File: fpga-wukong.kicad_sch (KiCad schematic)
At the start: 2 parts, among them J4 QMTECH FPGA Module U4, J5 QMTECH FPGA Module U5

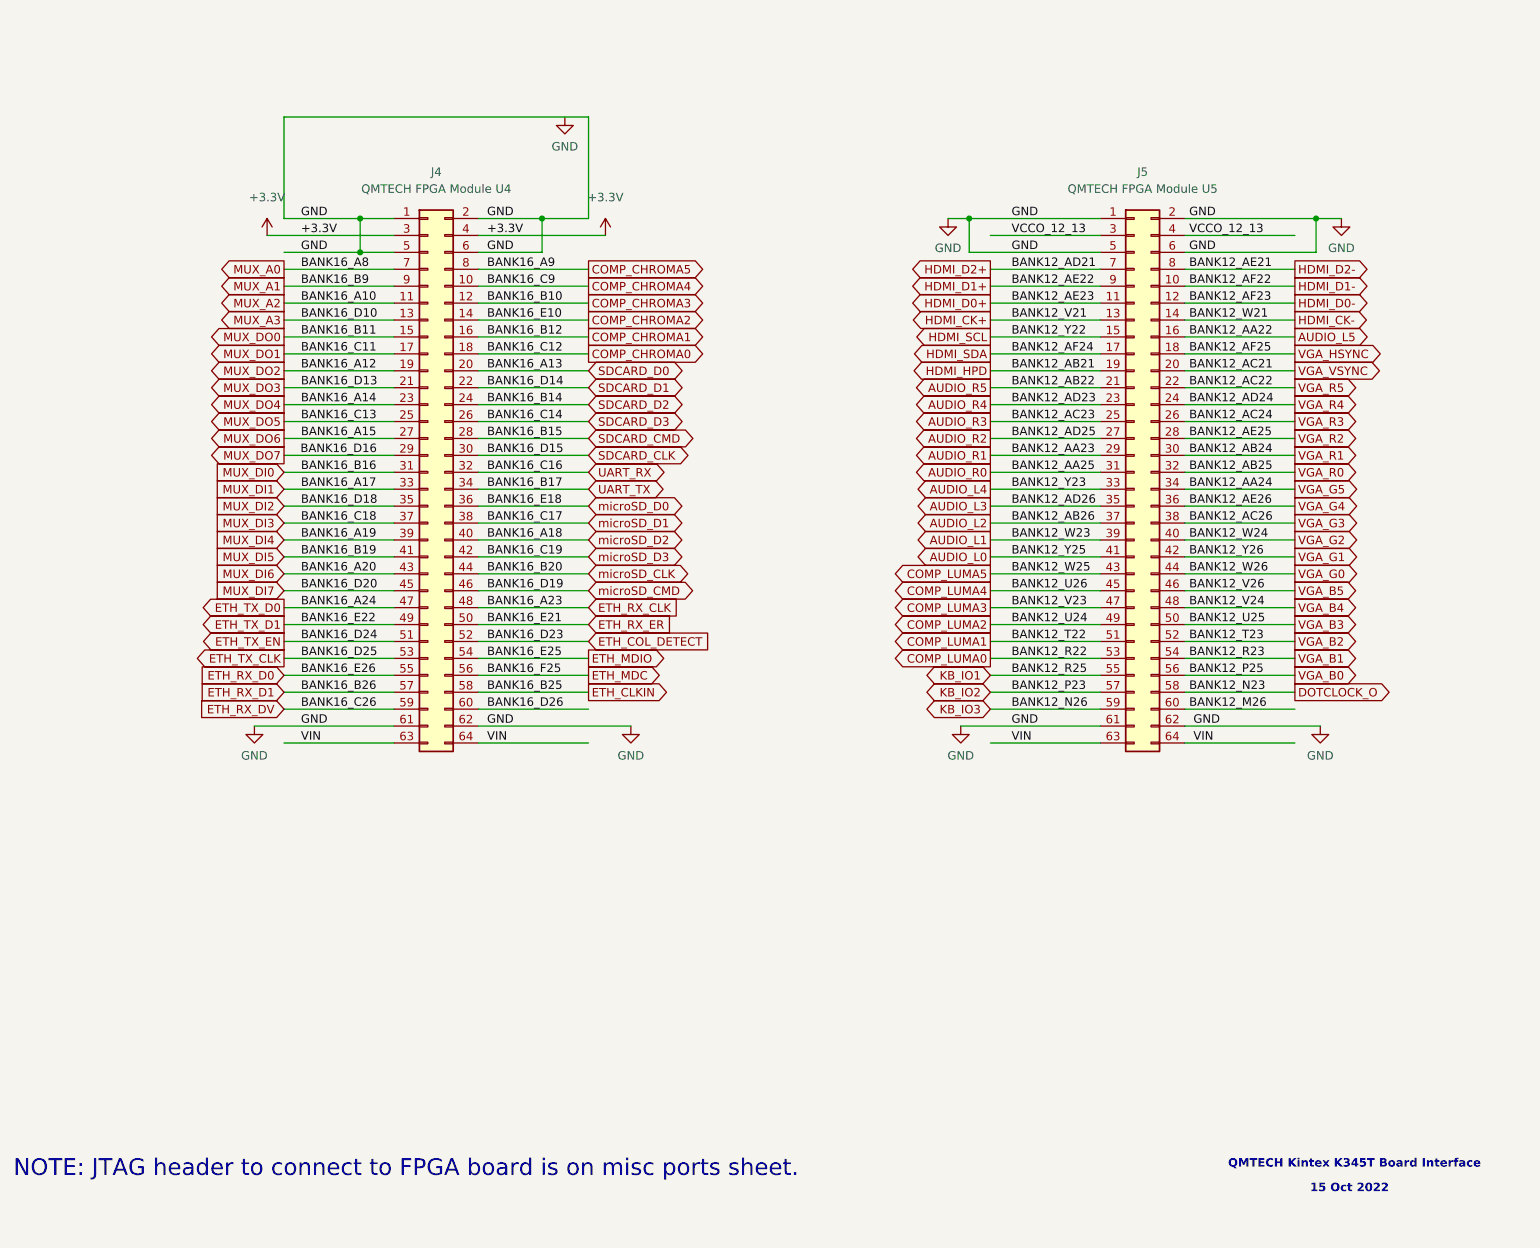
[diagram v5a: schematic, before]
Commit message: rearrange FPGA board connectors to detangle. Begin routing HDMI
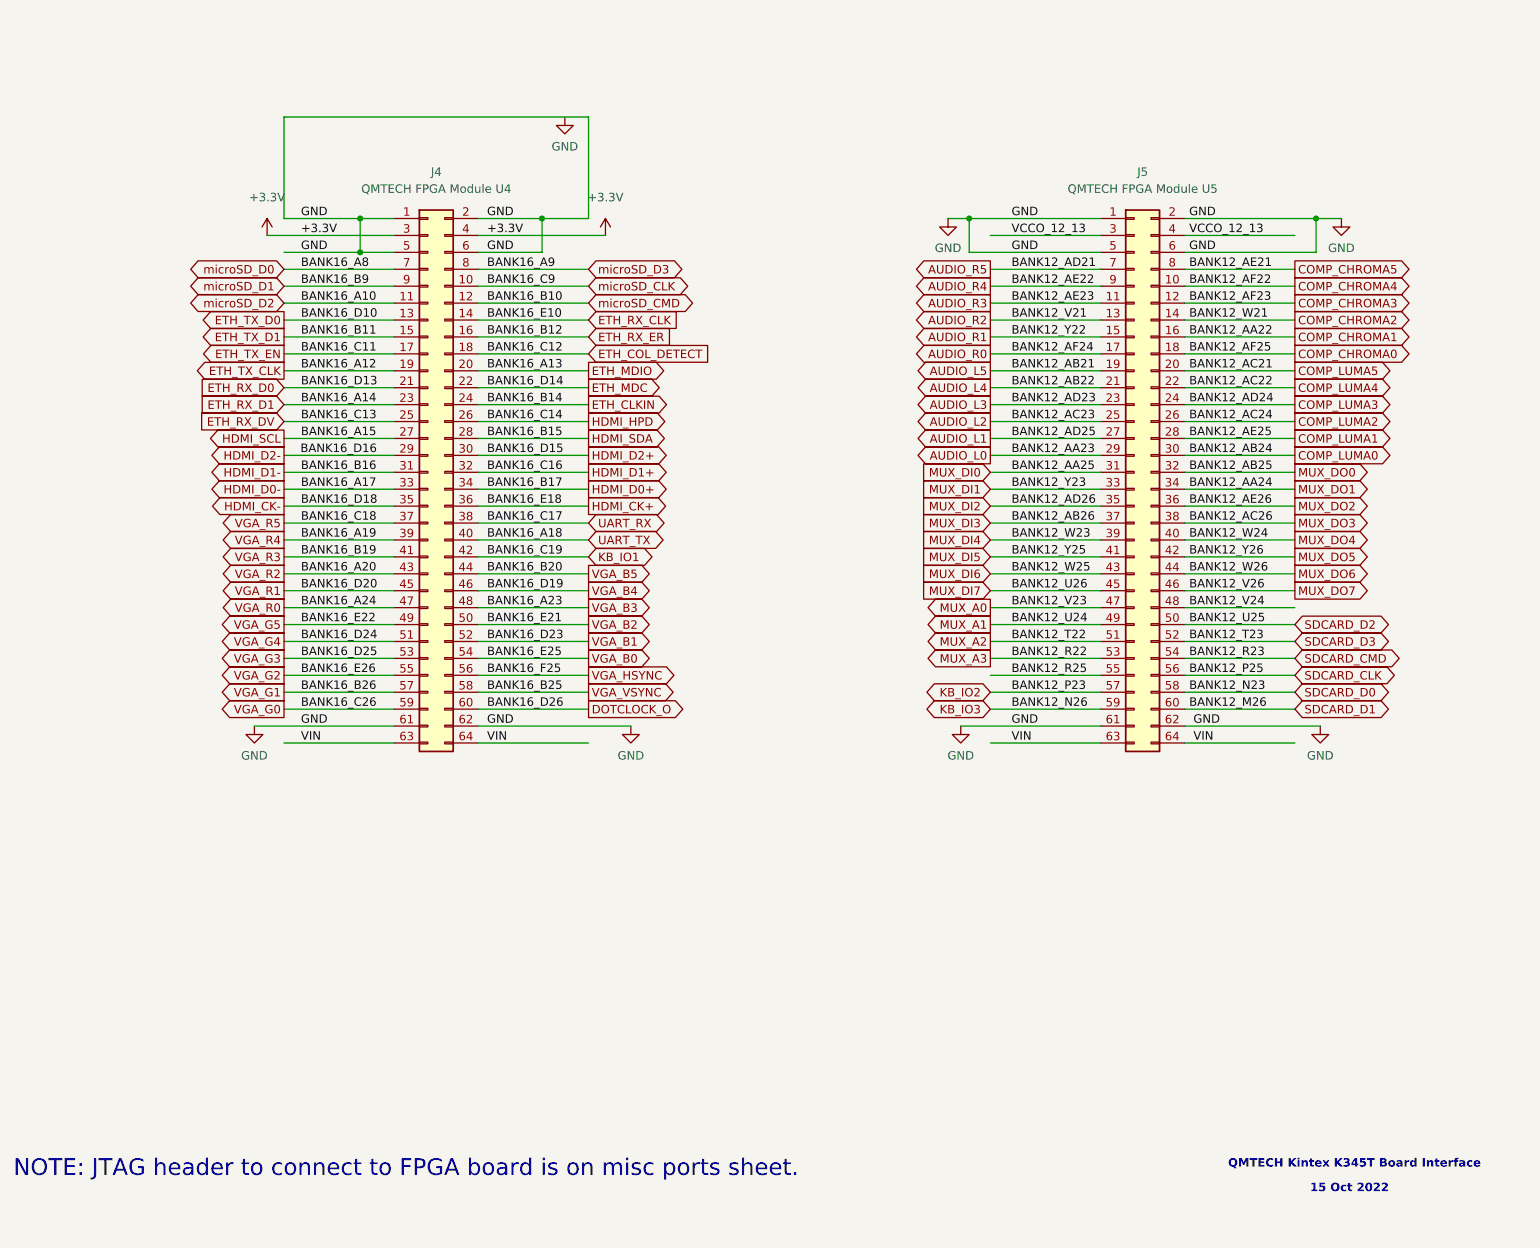
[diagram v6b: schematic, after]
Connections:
- net BANK12_M26 is gone; now on net SDCARD_D1: J5.60 (Pin_60)
- net BANK16_D26 is gone; now on net DOTCLOCK_O: J4.60 (Pin_60)
- net AUDIO_L0: now also J5.29 (Pin_29); no longer J5.41 (Pin_41)
- net AUDIO_L1: now also J5.27 (Pin_27); no longer J5.39 (Pin_39)
- net AUDIO_L2: now also J5.25 (Pin_25); no longer J5.37 (Pin_37)
- net AUDIO_L3: now also J5.23 (Pin_23); no longer J5.35 (Pin_35)
- net AUDIO_L4: now also J5.21 (Pin_21); no longer J5.33 (Pin_33)
- net AUDIO_L5: now also J5.19 (Pin_19); no longer J5.16 (Pin_16)
- net AUDIO_R0: now also J5.17 (Pin_17); no longer J5.31 (Pin_31)
- net AUDIO_R1: now also J5.15 (Pin_15); no longer J5.29 (Pin_29)
- net AUDIO_R2: now also J5.13 (Pin_13); no longer J5.27 (Pin_27)
- net AUDIO_R3: now also J5.11 (Pin_11); no longer J5.25 (Pin_25)
- net AUDIO_R4: now also J5.9 (Pin_9); no longer J5.23 (Pin_23)
- net AUDIO_R5: now also J5.7 (Pin_7); no longer J5.21 (Pin_21)
- net COMP_CHROMA0: now also J5.18 (Pin_18); no longer J4.18 (Pin_18)
- net COMP_CHROMA1: now also J5.16 (Pin_16); no longer J4.16 (Pin_16)
- net COMP_CHROMA2: now also J5.14 (Pin_14); no longer J4.14 (Pin_14)
- net COMP_CHROMA3: now also J5.12 (Pin_12); no longer J4.12 (Pin_12)
- net COMP_CHROMA4: now also J5.10 (Pin_10); no longer J4.10 (Pin_10)
- net COMP_CHROMA5: now also J5.8 (Pin_8); no longer J4.8 (Pin_8)
- net COMP_LUMA0: now also J5.30 (Pin_30); no longer J5.53 (Pin_53)
- net COMP_LUMA1: now also J5.28 (Pin_28); no longer J5.51 (Pin_51)
- net COMP_LUMA2: now also J5.26 (Pin_26); no longer J5.49 (Pin_49)
- net COMP_LUMA3: now also J5.24 (Pin_24); no longer J5.47 (Pin_47)
- net COMP_LUMA4: now also J5.22 (Pin_22); no longer J5.45 (Pin_45)
- net COMP_LUMA5: now also J5.20 (Pin_20); no longer J5.43 (Pin_43)
- net DOTCLOCK_O: no longer J5.58 (Pin_58)
- net ETH_CLKIN: now also J4.24 (Pin_24); no longer J4.58 (Pin_58)
- net ETH_COL_DETECT: now also J4.18 (Pin_18); no longer J4.52 (Pin_52)
- net ETH_MDC: now also J4.22 (Pin_22); no longer J4.56 (Pin_56)
- net ETH_MDIO: now also J4.20 (Pin_20); no longer J4.54 (Pin_54)
- net ETH_RX_CLK: now also J4.14 (Pin_14); no longer J4.48 (Pin_48)
- net ETH_RX_D0: now also J4.21 (Pin_21); no longer J4.55 (Pin_55)
- net ETH_RX_D1: now also J4.23 (Pin_23); no longer J4.57 (Pin_57)
- net ETH_RX_DV: now also J4.25 (Pin_25); no longer J4.59 (Pin_59)
- net ETH_RX_ER: now also J4.16 (Pin_16); no longer J4.50 (Pin_50)
- net ETH_TX_CLK: now also J4.19 (Pin_19); no longer J4.53 (Pin_53)
- net ETH_TX_D0: now also J4.13 (Pin_13); no longer J4.47 (Pin_47)
- net ETH_TX_D1: now also J4.15 (Pin_15); no longer J4.49 (Pin_49)
- net ETH_TX_EN: now also J4.17 (Pin_17); no longer J4.51 (Pin_51)
- net HDMI_CK+: now also J4.36 (Pin_36); no longer J5.13 (Pin_13)
- net HDMI_CK-: now also J4.35 (Pin_35); no longer J5.14 (Pin_14)
- net HDMI_D0+: now also J4.34 (Pin_34); no longer J5.11 (Pin_11)
- net HDMI_D0-: now also J4.33 (Pin_33); no longer J5.12 (Pin_12)
- net HDMI_D1+: now also J4.32 (Pin_32); no longer J5.9 (Pin_9)
- net HDMI_D1-: now also J4.31 (Pin_31); no longer J5.10 (Pin_10)
- net HDMI_D2+: now also J4.30 (Pin_30); no longer J5.7 (Pin_7)
- net HDMI_D2-: now also J4.29 (Pin_29); no longer J5.8 (Pin_8)
- net HDMI_HPD: now also J4.26 (Pin_26); no longer J5.19 (Pin_19)
- net HDMI_SCL: now also J4.27 (Pin_27); no longer J5.15 (Pin_15)
- net HDMI_SDA: now also J4.28 (Pin_28); no longer J5.17 (Pin_17)
- net KB_IO1: now also J4.42 (Pin_42); no longer J5.55 (Pin_55)
- net MUX_A0: now also J5.47 (Pin_47); no longer J4.7 (Pin_7)
- net MUX_A1: now also J5.49 (Pin_49); no longer J4.9 (Pin_9)
- net MUX_A2: now also J5.51 (Pin_51); no longer J4.11 (Pin_11)
- net MUX_A3: now also J5.53 (Pin_53); no longer J4.13 (Pin_13)
- net MUX_DI0: now also J5.31 (Pin_31); no longer J4.31 (Pin_31)
- net MUX_DI1: now also J5.33 (Pin_33); no longer J4.33 (Pin_33)
- net MUX_DI2: now also J5.35 (Pin_35); no longer J4.35 (Pin_35)
- net MUX_DI3: now also J5.37 (Pin_37); no longer J4.37 (Pin_37)
- net MUX_DI4: now also J5.39 (Pin_39); no longer J4.39 (Pin_39)
- net MUX_DI5: now also J5.41 (Pin_41); no longer J4.41 (Pin_41)
- net MUX_DI6: now also J5.43 (Pin_43); no longer J4.43 (Pin_43)
- net MUX_DI7: now also J5.45 (Pin_45); no longer J4.45 (Pin_45)
- net MUX_DO0: now also J5.32 (Pin_32); no longer J4.15 (Pin_15)
- net MUX_DO1: now also J5.34 (Pin_34); no longer J4.17 (Pin_17)
- net MUX_DO2: now also J5.36 (Pin_36); no longer J4.19 (Pin_19)
- net MUX_DO3: now also J5.38 (Pin_38); no longer J4.21 (Pin_21)
- net MUX_DO4: now also J5.40 (Pin_40); no longer J4.23 (Pin_23)
- net MUX_DO5: now also J5.42 (Pin_42); no longer J4.25 (Pin_25)
- net MUX_DO6: now also J5.44 (Pin_44); no longer J4.27 (Pin_27)
- net MUX_DO7: now also J5.46 (Pin_46); no longer J4.29 (Pin_29)
- net SDCARD_CLK: now also J5.56 (Pin_56); no longer J4.30 (Pin_30)
- net SDCARD_CMD: now also J5.54 (Pin_54); no longer J4.28 (Pin_28)
- net SDCARD_D0: now also J5.58 (Pin_58); no longer J4.20 (Pin_20)
- net SDCARD_D1: no longer J4.22 (Pin_22)
- net SDCARD_D2: now also J5.50 (Pin_50); no longer J4.24 (Pin_24)
- net SDCARD_D3: now also J5.52 (Pin_52); no longer J4.26 (Pin_26)
- net UART_RX: now also J4.38 (Pin_38); no longer J4.32 (Pin_32)
- net UART_TX: now also J4.40 (Pin_40); no longer J4.34 (Pin_34)
- net VGA_B0: now also J4.54 (Pin_54); no longer J5.56 (Pin_56)
- net VGA_B1: now also J4.52 (Pin_52); no longer J5.54 (Pin_54)
- net VGA_B2: now also J4.50 (Pin_50); no longer J5.52 (Pin_52)
- net VGA_B3: now also J4.48 (Pin_48); no longer J5.50 (Pin_50)
- net VGA_B4: now also J4.46 (Pin_46); no longer J5.48 (Pin_48)
- net VGA_B5: now also J4.44 (Pin_44); no longer J5.46 (Pin_46)
- net VGA_G0: now also J4.59 (Pin_59); no longer J5.44 (Pin_44)
- net VGA_G1: now also J4.57 (Pin_57); no longer J5.42 (Pin_42)
- net VGA_G2: now also J4.55 (Pin_55); no longer J5.40 (Pin_40)
- net VGA_G3: now also J4.53 (Pin_53); no longer J5.38 (Pin_38)
- net VGA_G4: now also J4.51 (Pin_51); no longer J5.36 (Pin_36)
- net VGA_G5: now also J4.49 (Pin_49); no longer J5.34 (Pin_34)
- net VGA_HSYNC: now also J4.56 (Pin_56); no longer J5.18 (Pin_18)
- net VGA_R0: now also J4.47 (Pin_47); no longer J5.32 (Pin_32)
- net VGA_R1: now also J4.45 (Pin_45); no longer J5.30 (Pin_30)
- net VGA_R2: now also J4.43 (Pin_43); no longer J5.28 (Pin_28)
- net VGA_R3: now also J4.41 (Pin_41); no longer J5.26 (Pin_26)
- net VGA_R4: now also J4.39 (Pin_39); no longer J5.24 (Pin_24)
- net VGA_R5: now also J4.37 (Pin_37); no longer J5.22 (Pin_22)
- net VGA_VSYNC: now also J4.58 (Pin_58); no longer J5.20 (Pin_20)
- net microSD_CLK: now also J4.10 (Pin_10); no longer J4.44 (Pin_44)
- net microSD_CMD: now also J4.12 (Pin_12); no longer J4.46 (Pin_46)
- net microSD_D0: now also J4.7 (Pin_7); no longer J4.36 (Pin_36)
- net microSD_D1: now also J4.9 (Pin_9); no longer J4.38 (Pin_38)
- net microSD_D2: now also J4.11 (Pin_11); no longer J4.40 (Pin_40)
- net microSD_D3: now also J4.8 (Pin_8); no longer J4.42 (Pin_42)
- new net BANK12_R25: J5.55 (Pin_55)
- new net BANK12_V24: J5.48 (Pin_48)

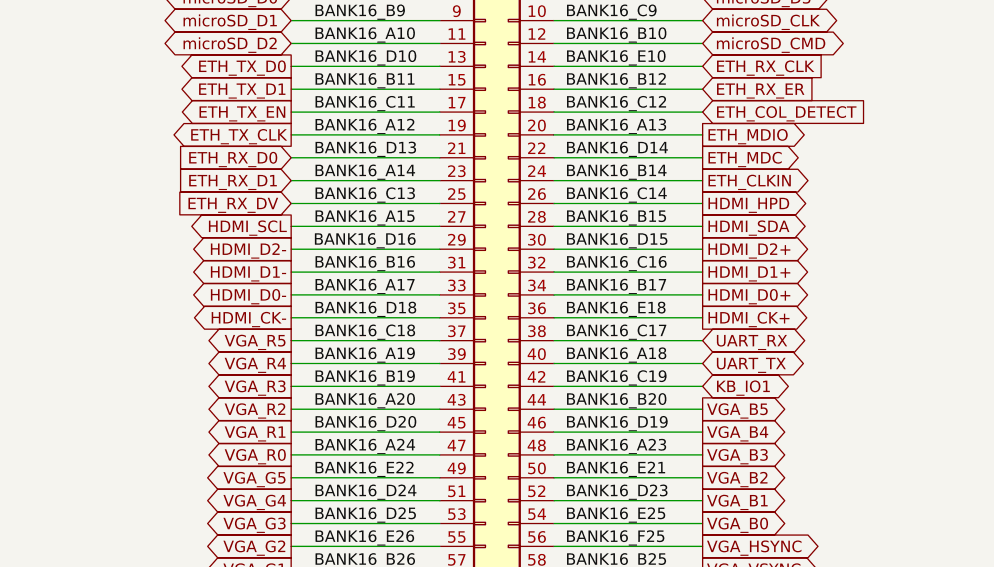
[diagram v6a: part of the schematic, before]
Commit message: Replace HDMI connector #13
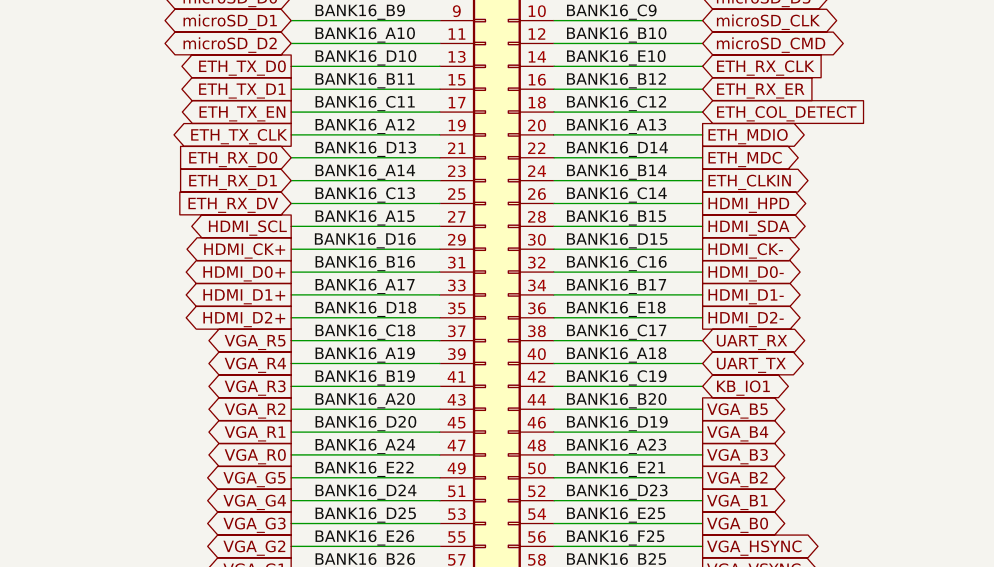
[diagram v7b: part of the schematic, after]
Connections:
- net HDMI_CK+: now also J4.29 (Pin_29); no longer J4.36 (Pin_36)
- net HDMI_CK-: now also J4.30 (Pin_30); no longer J4.35 (Pin_35)
- net HDMI_D0+: now also J4.31 (Pin_31); no longer J4.34 (Pin_34)
- net HDMI_D0-: now also J4.32 (Pin_32); no longer J4.33 (Pin_33)
- net HDMI_D1+: now also J4.33 (Pin_33); no longer J4.32 (Pin_32)
- net HDMI_D1-: now also J4.34 (Pin_34); no longer J4.31 (Pin_31)
- net HDMI_D2+: now also J4.35 (Pin_35); no longer J4.30 (Pin_30)
- net HDMI_D2-: now also J4.36 (Pin_36); no longer J4.29 (Pin_29)
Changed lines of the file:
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@@
     )
   )
-  (global_label "HDMI_D1-" (shape output) (at 60.325 85.725 180) (fields_autoplaced)
-    (effects (font (size 1.27 1.27)) (justify right))
-    (property "Intersheet References" "${INTERSHEET_REFS}" (id 0) (at 48.2357 85.6456 0)
-      (effects (font (size 1.27 1.27)) (justify right) hide)
+  (global_label "HDMI_D1-" (shape output) (at 106.045 88.265 0) (fields_autoplaced)
+    (effects (font (size 1.27 1.27)) (justify left))
+    (property "Intersheet References" "${INTERSHEET_REFS}" (id 0) (at 118.1343 88.3444 0)
+      (effects (font (size 1.27 1.27)) (justify left) hide)
     )
   )
@@
     )
   )
-  (global_label "HDMI_D0-" (shape output) (at 60.325 88.265 180) (fields_autoplaced)
-    (effects (font (size 1.27 1.27)) (justify right))
-    (property "Intersheet References" "${INTERSHEET_REFS}" (id 0) (at 48.2357 88.1856 0)
-      (effects (font (size 1.27 1.27)) (justify right) hide)
+  (global_label "HDMI_D0-" (shape output) (at 106.045 85.725 0) (fields_autoplaced)
+    (effects (font (size 1.27 1.27)) (justify left))
+    (property "Intersheet References" "${INTERSHEET_REFS}" (id 0) (at 118.1343 85.8044 0)
+      (effects (font (size 1.27 1.27)) (justify left) hide)
     )
   )
@@
     )
   )
-  (global_label "HDMI_D0+" (shape output) (at 106.045 88.265 0) (fields_autoplaced)
-    (effects (font (size 1.27 1.27)) (justify left))
-    (property "Intersheet References" "${INTERSHEET_REFS}" (id 0) (at 118.1343 88.1856 0)
-      (effects (font (size 1.27 1.27)) (justify left) hide)
+  (global_label "HDMI_D0+" (shape output) (at 60.325 85.725 180) (fields_autoplaced)
+    (effects (font (size 1.27 1.27)) (justify right))
+    (property "Intersheet References" "${INTERSHEET_REFS}" (id 0) (at 48.2357 85.8044 0)
+      (effects (font (size 1.27 1.27)) (justify right) hide)
     )
   )
@@
     )
   )
-  (global_label "HDMI_CK-" (shape output) (at 60.325 90.805 180) (fields_autoplaced)
-    (effects (font (size 1.27 1.27)) (justify right))
-    (property "Intersheet References" "${INTERSHEET_REFS}" (id 0) (at 48.1752 90.7256 0)
-      (effects (font (size 1.27 1.27)) (justify right) hide)
+  (global_label "HDMI_CK-" (shape output) (at 106.045 83.185 0) (fields_autoplaced)
+    (effects (font (size 1.27 1.27)) (justify left))
+    (property "Intersheet References" "${INTERSHEET_REFS}" (id 0) (at 118.1948 83.2644 0)
+      (effects (font (size 1.27 1.27)) (justify left) hide)
     )
   )
@@
     )
   )
-  (global_label "HDMI_CK+" (shape output) (at 106.045 90.805 0) (fields_autoplaced)
-    (effects (font (size 1.27 1.27)) (justify left))
-    (property "Intersheet References" "${INTERSHEET_REFS}" (id 0) (at 118.1948 90.7256 0)
-      (effects (font (size 1.27 1.27)) (justify left) hide)
+  (global_label "HDMI_CK+" (shape output) (at 60.325 83.185 180) (fields_autoplaced)
+    (effects (font (size 1.27 1.27)) (justify right))
+    (property "Intersheet References" "${INTERSHEET_REFS}" (id 0) (at 48.1752 83.2644 0)
+      (effects (font (size 1.27 1.27)) (justify right) hide)
     )
   )
@@
     )
   )
-  (global_label "HDMI_D1+" (shape output) (at 106.045 85.725 0) (fields_autoplaced)
-    (effects (font (size 1.27 1.27)) (justify left))
-    (property "Intersheet References" "${INTERSHEET_REFS}" (id 0) (at 118.1343 85.6456 0)
-      (effects (font (size 1.27 1.27)) (justify left) hide)
+  (global_label "HDMI_D1+" (shape output) (at 60.325 88.265 180) (fields_autoplaced)
+    (effects (font (size 1.27 1.27)) (justify right))
+    (property "Intersheet References" "${INTERSHEET_REFS}" (id 0) (at 48.2357 88.3444 0)
+      (effects (font (size 1.27 1.27)) (justify right) hide)
     )
   )
@@
     )
   )
-  (global_label "HDMI_D2+" (shape output) (at 106.045 83.185 0) (fields_autoplaced)
-    (effects (font (size 1.27 1.27)) (justify left))
-    (property "Intersheet References" "${INTERSHEET_REFS}" (id 0) (at 118.1343 83.1056 0)
-      (effects (font (size 1.27 1.27)) (justify left) hide)
+  (global_label "HDMI_D2+" (shape output) (at 60.325 90.805 180) (fields_autoplaced)
+    (effects (font (size 1.27 1.27)) (justify right))
+    (property "Intersheet References" "${INTERSHEET_REFS}" (id 0) (at 48.2357 90.8844 0)
+      (effects (font (size 1.27 1.27)) (justify right) hide)
     )
   )
@@
     )
   )
-  (global_label "HDMI_D2-" (shape output) (at 60.325 83.185 180) (fields_autoplaced)
-    (effects (font (size 1.27 1.27)) (justify right))
-    (property "Intersheet References" "${INTERSHEET_REFS}" (id 0) (at 48.2357 83.1056 0)
-      (effects (font (size 1.27 1.27)) (justify right) hide)
-    )
-  )
+  (global_label "HDMI_D2-" (shape output) (at 106.045 90.805 0) (fields_autoplaced)
+    (effects (font (size 1.27 1.27)) (justify left))
+    (property "Intersheet References" "${INTERSHEET_REFS}" (id 0) (at 118.1343 90.8844 0)
+      (effects (font (size 1.27 1.27)) (justify left) hide)
+    )
+  )
